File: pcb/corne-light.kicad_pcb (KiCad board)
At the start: 2 copper layers, 275.5 x 105.6 mm, 122 parts, among them J1 MJ-4PP-9, J2 OLED, J5 Breakaway_Tabs, J6 MJ-4PP-9, J7 OLED, SW1 SW_PUSH, SW10 SW_PUSH, SW11 SW_PUSH, SW12 SW_PUSH, SW13 SW_PUSH, SW14 SW_PUSH, SW15 SW_PUSH, SW16 SW_PUSH, SW17 SW_PUSH, SW18 SW_PUSH, SW19 Rotary_Encoder_Switch, SW2 SW_PUSH, SW20 SW_PUSH, SW21 SW_PUSH, SW22 SW_PUSH, SW23 SW_PUSH, SW24 SW_PUSH, SW25 SW_PUSH, SW26 SW_PUSH, SW27 SW_PUSH, SW28 SW_PUSH, SW29 SW_PUSH, SW3 SW_PUSH, SW30 SW_PUSH, SW31 SW_PUSH, SW32 SW_PUSH, SW33 SW_PUSH, SW34 SW_PUSH, SW35 SW_PUSH, SW36 SW_PUSH, SW37 SW_PUSH, SW38 SW_PUSH, SW39 SW_PUSH, SW4 SW_PUSH, SW40 Rotary_Encoder_Switch, SW41 SW_PUSH, SW42 SW_PUSH, SW5 SW_PUSH, SW6 SW_PUSH, SW7 SW_PUSH, SW8 SW_PUSH, SW9 SW_PUSH, U1 ProMicro, U2 ProMicro

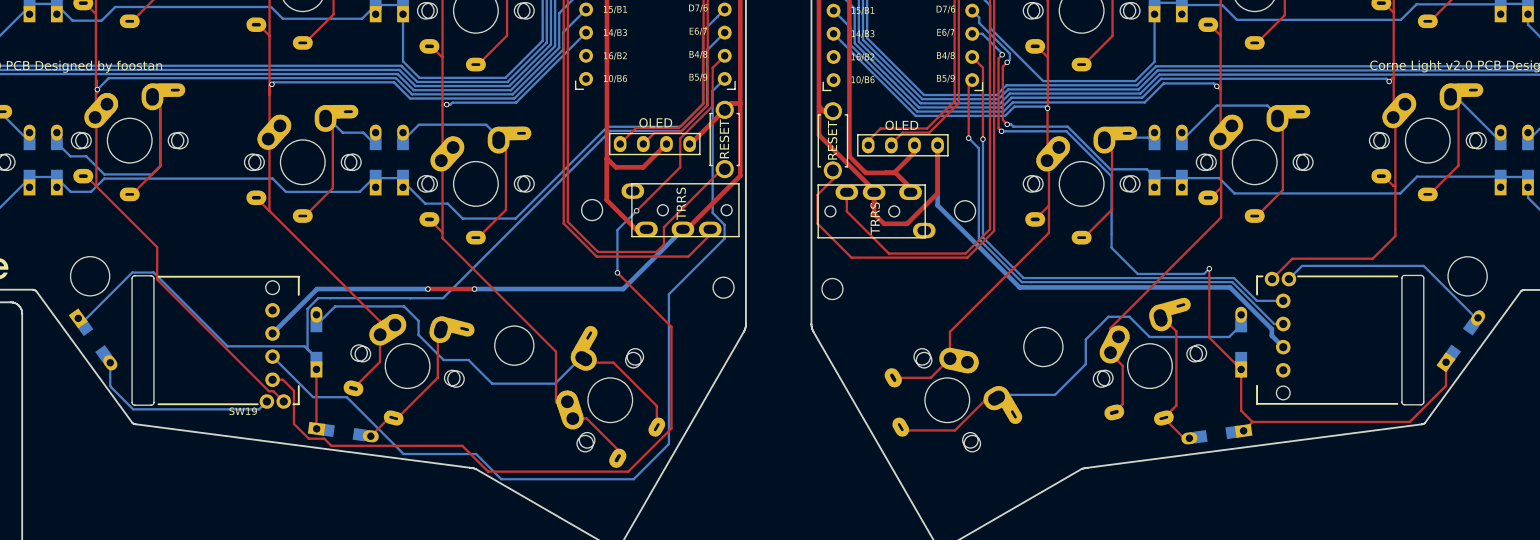
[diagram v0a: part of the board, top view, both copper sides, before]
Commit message: Update rotation and proper grounding
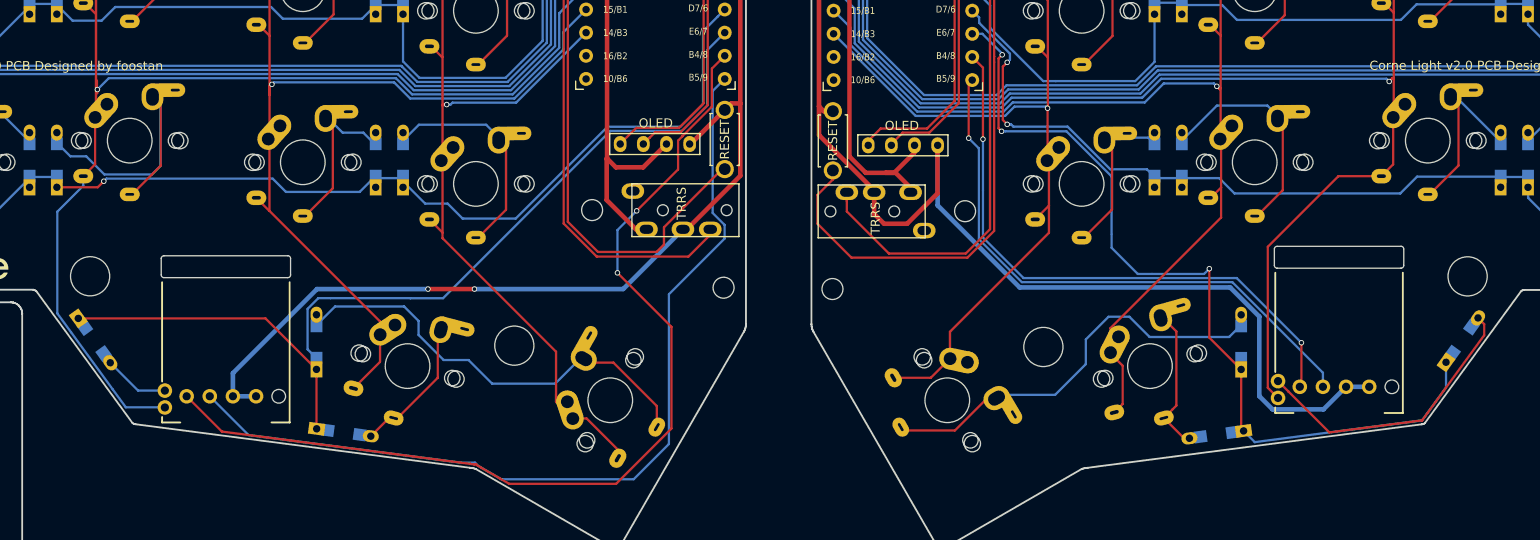
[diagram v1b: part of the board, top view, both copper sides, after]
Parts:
- turned SW19 to 90 degrees
- turned SW40 to 90 degrees
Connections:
- SW19 pad D: (no net) -> GND
- SW40 pad D: (no net) -> GNDA
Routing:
- net GNDA: track 129.5 -> 147.5 mm
- net Net-(D19-Pad2): track 21.2 -> 8.55 mm
- net GND: track 116.4 -> 127.6 mm
- net col3_r: track 143.4 -> 153.1 mm
- net ENCA_r: track 56.2 -> 65.0 mm, vias 1 -> 2
- net Net-(D40-Pad2): track 25.0 -> 33.8 mm
- net ENCB_r: track 55.4 -> 63.5 mm
- net ENCA: track 100.3 -> 106.4 mm
- net ENCB: track 94.4 -> 98.2 mm
- net row3: track 108.0 -> 106.3 mm
- net Net-(D20-Pad2): track 15.7 -> 17.0 mm
- net row3_r: track 96.6 -> 97.8 mm
- net col3: track 148.0 -> 146.9 mm
- net row2: track 153.9 -> 152.9 mm, vias 0 -> 1

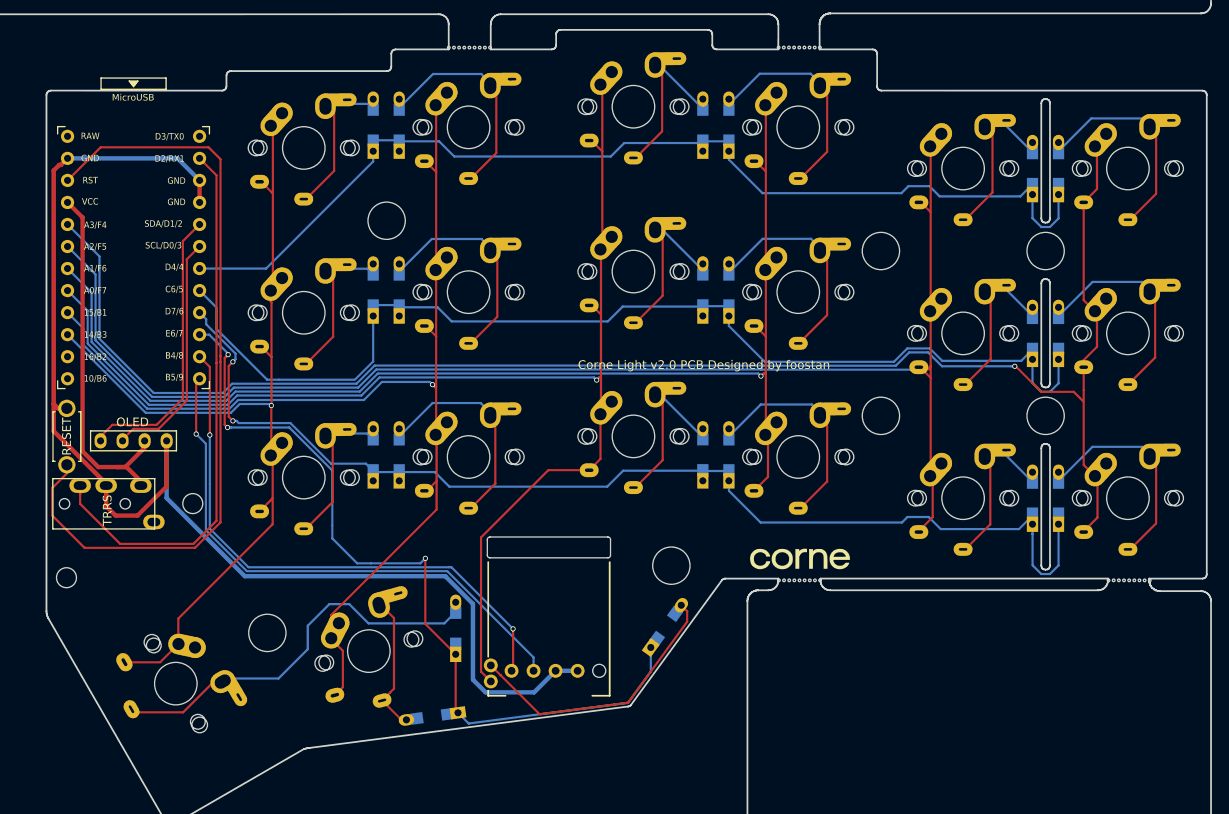
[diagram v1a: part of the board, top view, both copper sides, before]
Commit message: finish alps and leds on right half
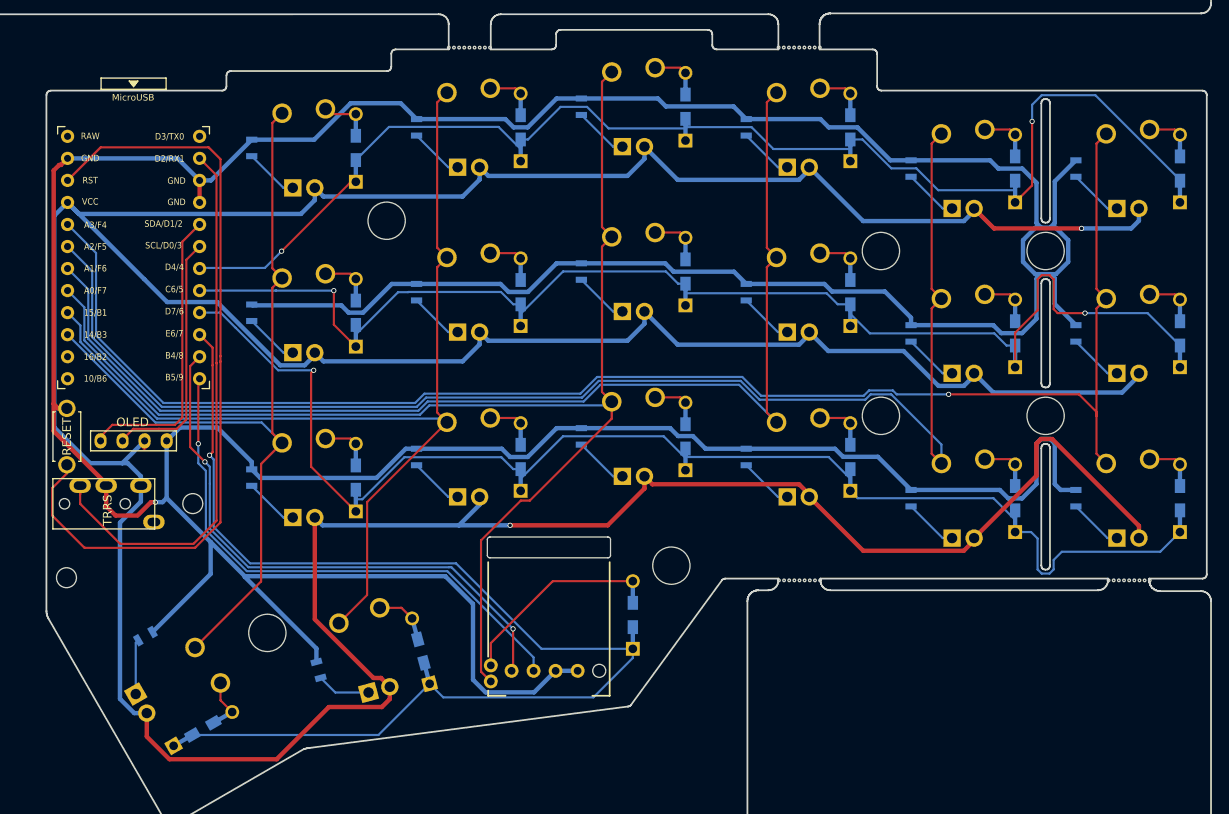
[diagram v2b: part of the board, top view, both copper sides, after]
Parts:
- removed D22, D23, D24, D25, D26, D27, D28, D29, D30, D31, D32, D33, D34, D35, D36, D37, D38, D39, D40, D41, D42: D, kbd:D3_TH_SMD_v2
- removed the G*** at (241.0, 91.0)
- removed the G*** at (240.8, 91.0)
- removed SW22, SW23, SW24, SW25, SW26, SW27, SW28, SW29, SW30, SW31, SW32, SW33, SW34, SW35, SW36, SW37, SW38, SW39, SW41: SW_PUSH, kbd:keyswitch_cherrymx_alps_choc12_1u
- removed SW42: SW_PUSH, kbd:keyswitch_cherrymx_alps_choc12_1.5u
- added D43: D_Small, Keebio-Parts:Diode-Hybrid-Back, F.Cu at (284.7, 45.9)
- added D44: D_Small, Keebio-Parts:Diode-Hybrid-Back, F.Cu at (284.7, 64.9)
- added D45: D_Small, Keebio-Parts:Diode-Hybrid-Back, F.Cu at (284.7, 83.9)
- added D46: D_Small, Keebio-Parts:Diode-Hybrid-Back, F.Cu at (265.7, 45.9)
- added D47: D_Small, Keebio-Parts:Diode-Hybrid-Back, F.Cu at (265.7, 64.9)
- added D48: D_Small, Keebio-Parts:Diode-Hybrid-Back, F.Cu at (265.7, 83.9)
- added D49: D_Small, Keebio-Parts:Diode-Hybrid-Back, F.Cu at (246.7, 41.2)
- added D50: D_Small, Keebio-Parts:Diode-Hybrid-Back, F.Cu at (246.7, 60.2)
- added D51: D_Small, Keebio-Parts:Diode-Hybrid-Back, F.Cu at (246.7, 79.2)
- added D52: D_Small, Keebio-Parts:Diode-Hybrid-Back, F.Cu at (227.7, 38.8)
- added D53: D_Small, Keebio-Parts:Diode-Hybrid-Back, F.Cu at (227.7, 57.8)
- added D54: D_Small, Keebio-Parts:Diode-Hybrid-Back, F.Cu at (227.7, 76.8)
- added D55: D_Small, Keebio-Parts:Diode-Hybrid-Back, F.Cu at (208.7, 41.2)
- added D56: D_Small, Keebio-Parts:Diode-Hybrid-Back, F.Cu at (208.7, 60.2)
- added D57: D_Small, Keebio-Parts:Diode-Hybrid-Back, F.Cu at (208.7, 79.2)
- added D58: D_Small, Keebio-Parts:Diode-Hybrid-Back, F.Cu at (189.7, 43.5)
- added D59: D_Small, Keebio-Parts:Diode-Hybrid-Back, F.Cu at (189.7, 62.5)
- added D60: D_Small, Keebio-Parts:Diode-Hybrid-Back, F.Cu at (189.7, 81.5)
- added D61: D_Small, Keebio-Parts:Diode-Hybrid-Back, F.Cu at (221.6, 97.4)
- added D62: D_Small, Keebio-Parts:Diode-Hybrid-Back, F.Cu at (197.2, 101.5)
- added D63: D_Small, Keebio-Parts:Diode-Hybrid-Back, F.Cu at (172.1, 110.5)
- added MX1: MX-LED, Alps_Only:ALPS-1U-LED, F.Cu at (278.7, 45.9)
- added MX10: MX-LED, Alps_Only:ALPS-1U-LED, F.Cu at (221.7, 38.8)
- added MX11: MX-LED, Alps_Only:ALPS-1U-LED, F.Cu at (221.7, 57.8)
- added MX12: MX-LED, Alps_Only:ALPS-1U-LED, F.Cu at (221.7, 76.8)
- added MX13: MX-LED, Alps_Only:ALPS-1U-LED, F.Cu at (202.7, 41.2)
- added MX14: MX-LED, Alps_Only:ALPS-1U-LED, F.Cu at (202.7, 60.2)
- added MX15: MX-LED, Alps_Only:ALPS-1U-LED, F.Cu at (202.7, 79.2)
- added MX16: MX-LED, Alps_Only:ALPS-1U-LED, F.Cu at (183.7, 43.5)
- added MX17: MX-LED, Alps_Only:ALPS-1U-LED, F.Cu at (183.7, 62.5)
- added MX18: MX-LED, Alps_Only:ALPS-1U-LED, F.Cu at (183.7, 81.5)
- added MX19: MX-LED, Alps_Only:ALPS-1U-LED, F.Cu at (191.2, 101.5)
- added MX2: MX-LED, Alps_Only:ALPS-1U-LED, F.Cu at (278.7, 64.9)
- added MX20: MX-LED, Alps_Only:ALPS-1.5U-LED, F.Cu at (168.9, 105.3)
- added MX3: MX-LED, Alps_Only:ALPS-1U-LED, F.Cu at (278.7, 83.9)
- added MX4: MX-LED, Alps_Only:ALPS-1U-LED, F.Cu at (259.7, 45.9)
- added MX5: MX-LED, Alps_Only:ALPS-1U-LED, F.Cu at (259.7, 64.9)
- added MX6: MX-LED, Alps_Only:ALPS-1U-LED, F.Cu at (259.7, 83.9)
- added MX7: MX-LED, Alps_Only:ALPS-1U-LED, F.Cu at (240.7, 41.2)
- added MX8: MX-LED, Alps_Only:ALPS-1U-LED, F.Cu at (240.7, 60.2)
- added MX9: MX-LED, Alps_Only:ALPS-1U-LED, F.Cu at (240.7, 79.2)
- added R1: 470, Keebio-Parts:R_0805, B.Cu at (272.7, 45.9)
- added R10: 470, Keebio-Parts:R_0805, B.Cu at (215.7, 38.8)
- added R11: 470, Keebio-Parts:R_0805, B.Cu at (215.7, 57.8)
- added R12: 470, Keebio-Parts:R_0805, B.Cu at (215.7, 76.8)
- added R13: 470, Keebio-Parts:R_0805, B.Cu at (196.7, 41.2)
- added R14: 470, Keebio-Parts:R_0805, B.Cu at (196.7, 60.2)
- added R15: 470, Keebio-Parts:R_0805, B.Cu at (196.7, 79.2)
- added R16: 470, Keebio-Parts:R_0805, B.Cu at (177.7, 43.5)
- added R17: 470, Keebio-Parts:R_0805, B.Cu at (177.7, 62.5)
- added R18: 470, Keebio-Parts:R_0805, B.Cu at (177.7, 81.5)
- added R19: 470, Keebio-Parts:R_0805, B.Cu at (185.4, 103.7)
- added R2: 470, Keebio-Parts:R_0805, B.Cu at (272.7, 64.9)
- added R20: 470, Keebio-Parts:R_0805, B.Cu at (165.4, 99.8)
- added R3: 470, Keebio-Parts:R_0805, B.Cu at (272.7, 83.9)
- added R4: 470, Keebio-Parts:R_0805, B.Cu at (253.7, 45.9)
- added R5: 470, Keebio-Parts:R_0805, B.Cu at (253.7, 64.9)
- added R6: 470, Keebio-Parts:R_0805, B.Cu at (253.7, 83.9)
- added R7: 470, Keebio-Parts:R_0805, B.Cu at (234.7, 41.2)
- added R8: 470, Keebio-Parts:R_0805, B.Cu at (234.7, 60.2)
- added R9: 470, Keebio-Parts:R_0805, B.Cu at (234.7, 79.2)
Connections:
- SW19 pad D: GND -> (no net)
- SW40 pad D: GNDA -> (no net)
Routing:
- net VDD: track 43.0 -> 539.2 mm, vias 0 -> 2
- net GNDA: track 147.5 -> 543.6 mm, vias 0 -> 1
- net Net-(D42-Pad2): track 47.8 -> 0.00 mm
- net row3_r: track 97.8 -> 134.1 mm, vias 3 -> 1
- net Net-(D24-Pad2): track 27.6 -> 0.00 mm
- net Net-(D32-Pad2): track 27.5 -> 0.00 mm
- net Net-(D26-Pad2): track 27.4 -> 0.00 mm
- net Net-(D38-Pad2): track 27.3 -> 0.00 mm
- net Net-(D36-Pad2): track 27.2 -> 0.00 mm
- net Net-(D34-Pad2): track 27.2 -> 0.00 mm
- net Net-(D30-Pad2): track 27.1 -> 0.00 mm
- net Net-(D22-Pad2): track 27.1 -> 0.00 mm
- net Net-(D28-Pad2): track 27.0 -> 0.00 mm
- net Net-(D31-Pad2): track 22.6 -> 0.00 mm
- net Net-(D25-Pad2): track 22.3 -> 0.00 mm
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
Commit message: add alps and leds to left half
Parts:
- removed G*** (x2): LOGO, kbd:corne-logo-horizontal
- removed SW10, SW11, SW12, SW13, SW14, SW15, SW16, SW17, SW18, SW2, SW20, SW3, SW4, SW5, SW6, SW7, SW8, SW9: SW_PUSH, kbd:keyswitch_cherrymx_alps_choc12_1u
- removed SW19: Rotary_Encoder_Switch, Encoder:RollerEncoder_Panasonic_EVQWGD001
- removed SW21: SW_PUSH, kbd:keyswitch_cherrymx_alps_choc12_1.5u
- added MX21: MX-LED, Alps_Only:ALPS-1U-LED, F.Cu at (22.2, 45.9)
- added MX22: MX-LED, Alps_Only:ALPS-1U-LED, F.Cu at (22.2, 64.9)
- added MX23: MX-LED, Alps_Only:ALPS-1U-LED, F.Cu at (22.2, 83.9)
- added MX24: MX-LED, Alps_Only:ALPS-1U-LED, F.Cu at (41.2, 45.9)
- added MX25: MX-LED, Alps_Only:ALPS-1U-LED, F.Cu at (41.2, 64.9)
- added MX26: MX-LED, Alps_Only:ALPS-1U-LED, F.Cu at (41.2, 83.9)
- added MX27: MX-LED, Alps_Only:ALPS-1U-LED, F.Cu at (60.2, 41.2)
- added MX28: MX-LED, Alps_Only:ALPS-1U-LED, F.Cu at (60.2, 60.2)
- added MX29: MX-LED, Alps_Only:ALPS-1U-LED, F.Cu at (60.2, 79.2)
- added MX30: MX-LED, Alps_Only:ALPS-1U-LED, F.Cu at (79.2, 38.8)
- added MX31: MX-LED, Alps_Only:ALPS-1U-LED, F.Cu at (79.2, 57.8)
- added MX32: MX-LED, Alps_Only:ALPS-1U-LED, F.Cu at (79.2, 76.8)
- added MX33: MX-LED, Alps_Only:ALPS-1U-LED, F.Cu at (98.2, 41.2)
- added MX34: MX-LED, Alps_Only:ALPS-1U-LED, F.Cu at (98.2, 60.2)
- added MX35: MX-LED, Alps_Only:ALPS-1U-LED, F.Cu at (98.2, 79.2)
- added MX36: MX-LED, Alps_Only:ALPS-1U-LED, F.Cu at (109.7, 101.5)
- added MX37: MX-LED, Alps_Only:ALPS-1U-LED, F.Cu at (117.2, 43.5)
- added MX38: MX-LED, Alps_Only:ALPS-1U-LED, F.Cu at (117.2, 62.5)
- added MX39: MX-LED, Alps_Only:ALPS-1U-LED, F.Cu at (117.2, 81.5)
- added MX40: MX-LED, Alps_Only:ALPS-1.5U-LED, F.Cu at (131.9, 105.3)
- added Q1: Q_NPN_BEC, Package_TO_SOT_SMD:SOT-23, B.Cu at (164.8, 43.4)
- added Q2: Q_NPN_BEC, Package_TO_SOT_SMD:SOT-23, B.Cu at (135.3, 42.0)
- added R21: 1k, Keebio-Parts:R_0805, B.Cu at (160.4, 44.3)
- added R22: 1k, Keebio-Parts:R_0805, B.Cu at (138.8, 42.0)
- added R23: 470, Keebio-Parts:R_0805, B.Cu at (16.2, 45.9)
- added R24: 470, Keebio-Parts:R_0805, B.Cu at (16.2, 64.9)
- added R25: 470, Keebio-Parts:R_0805, B.Cu at (16.2, 83.9)
- added R26: 470, Keebio-Parts:R_0805, B.Cu at (35.2, 45.9)
- added R27: 470, Keebio-Parts:R_0805, B.Cu at (35.2, 64.9)
- added R28: 470, Keebio-Parts:R_0805, B.Cu at (35.2, 83.9)
- added R29: 470, Keebio-Parts:R_0805, B.Cu at (54.2, 41.2)
- added R30: 470, Keebio-Parts:R_0805, B.Cu at (54.2, 60.2)
- added R31: 470, Keebio-Parts:R_0805, B.Cu at (54.2, 79.2)
- added R32: 470, Keebio-Parts:R_0805, B.Cu at (73.2, 38.8)
- added R33: 470, Keebio-Parts:R_0805, B.Cu at (73.2, 57.8)
- added R34: 470, Keebio-Parts:R_0805, B.Cu at (73.2, 76.8)
- added R35: 470, Keebio-Parts:R_0805, B.Cu at (92.2, 41.2)
- added R36: 470, Keebio-Parts:R_0805, B.Cu at (92.2, 60.2)
- added R37: 470, Keebio-Parts:R_0805, B.Cu at (92.2, 79.2)
- added R38: 470, Keebio-Parts:R_0805, B.Cu at (104.0, 100.4)
- added R39: 470, Keebio-Parts:R_0805, B.Cu at (111.2, 43.5)
- added R40: 470, Keebio-Parts:R_0805, B.Cu at (111.2, 62.5)
- added R41: 470, Keebio-Parts:R_0805, B.Cu at (111.2, 81.5)
- added R42: 470, Keebio-Parts:R_0805, B.Cu at (129.5, 110.6)
- D1, D10, D11, D12, D13, D14, D15, D16, D17, D18, D19, D2, D20, D21, D3, D4, D5, D6, D7, D8, D9: value D -> D_Small; footprint kbd:D3_TH_SMD_v2 -> Keebio-Parts:Diode-Hybrid-Back; moved to F.Cu
- SW1: value SW_PUSH -> Rotary_Encoder_Switch; footprint kbd:keyswitch_cherrymx_alps_choc12_1u -> Encoder:RollerEncoder_Panasonic_EVQWGD001
- moved SW1 85.7 mm to (89.3, 99.2), turned to 90 degrees
- moved D14 82.9 mm to (104.2, 41.2), turned to 270 degrees
- moved D6 75.5 mm to (47.2, 83.9), turned to 270 degrees
- moved D5 63.7 mm to (47.2, 64.9), turned to 270 degrees
- moved D19 60.0 mm to (123.2, 62.5), turned to 270 degrees
- moved D3 58.7 mm to (28.2, 83.9), turned to 270 degrees
- moved D13 51.8 mm to (80.2, 97.6)
- moved D7 43.1 mm to (66.2, 41.2), turned to 270 degrees
- moved D15 40.6 mm to (104.2, 60.2), turned to 270 degrees
- moved D18 38.0 mm to (123.2, 43.5), turned to 270 degrees
- moved D21 35.3 mm to (135.0, 100.2), turned to 330 degrees
- moved D20 34.1 mm to (123.2, 81.5), turned to 270 degrees
- moved D8 33.3 mm to (66.2, 60.2), turned to 270 degrees
- moved D16 33.0 mm to (104.2, 79.2), turned to 270 degrees
- moved D12 29.3 mm to (85.2, 76.8), turned to 270 degrees
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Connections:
- D10 pad 1: row1 -> row0
- D12 pad 1: row1 -> row2
- D13 pad 1: row2 -> row3
- D14 pad 1: row2 -> row0
- D15 pad 1: row2 -> row1
- D17 pad 1: row2 -> row3
- D18 pad 1: row2 -> row0
- D19 pad 1: row3 -> row1
- D2 pad 1: row0 -> row1
- D20 pad 1: row3 -> row2
- D3 pad 1: row0 -> row2
- D5 pad 1: row0 -> row1
- D6 pad 1: row0 -> row2
- D7 pad 1: row1 -> row0
- D9 pad 1: row1 -> row2
- R1 pad 2: GNDA -> PWM_r
- R10 pad 2: GNDA -> PWM_r
- R11 pad 2: GNDA -> PWM_r
- R12 pad 2: GNDA -> PWM_r
- R13 pad 2: GNDA -> PWM_r
- R14 pad 2: GNDA -> PWM_r
- R15 pad 2: GNDA -> PWM_r
- R16 pad 2: GNDA -> PWM_r
- R17 pad 2: GNDA -> PWM_r
- R18 pad 2: GNDA -> PWM_r
- R19 pad 2: GNDA -> PWM_r
- R2 pad 2: GNDA -> PWM_r
- R20 pad 2: GNDA -> PWM_r
- R3 pad 2: GNDA -> PWM_r
- R4 pad 2: GNDA -> PWM_r
- R5 pad 2: GNDA -> PWM_r
- R6 pad 2: GNDA -> PWM_r
- R7 pad 2: GNDA -> PWM_r
- R8 pad 2: GNDA -> PWM_r
- R9 pad 2: GNDA -> PWM_r
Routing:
- net PWM: track 0.00 -> 446.6 mm, vias 0 -> 6
- net VCC: track 48.3 -> 490.5 mm, vias 0 -> 2
- net PWM_r: track 0.00 -> 429.0 mm, vias 0 -> 3
- net GNDA: track 543.6 -> 146.0 mm, vias 1 -> 0
- net Net-(D21-Pad2): track 49.4 -> 4.48 mm
- net Net-(R22-Pad2): track 0.00 -> 35.2 mm, vias 0 -> 2
- net data: track 78.9 -> 44.5 mm
- net Net-(D16-Pad2): track 35.7 -> 5.28 mm
- net Net-(R21-Pad2): track 0.00 -> 27.1 mm, vias 0 -> 1
- net col0: track 182.3 -> 155.4 mm, vias 1 -> 0
- net row1: track 164.0 -> 137.8 mm, vias 0 -> 1
- net Net-(D4-Pad2): track 29.0 -> 5.30 mm
- net Net-(D10-Pad2): track 27.9 -> 5.24 mm
- net Net-(D14-Pad2): track 27.9 -> 5.28 mm
- net Net-(D2-Pad2): track 27.4 -> 5.26 mm
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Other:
- board text removed: "Corne Light v2.0 PCB Designed by foostan"

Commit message: Finish RGB
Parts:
- added LED1: YS-SK6812MINI-E, Keebio-Parts:SK6812-MINI-E, F.Cu at (163.8, 63.1)
- added LED10: YS-SK6812MINI-E, Keebio-Parts:SK6812-MINI-E, F.Cu at (86.6, 46.7)
- added LED2: YS-SK6812MINI-E, Keebio-Parts:SK6812-MINI-E, F.Cu at (167.5, 93.1)
- added LED3: YS-SK6812MINI-E, Keebio-Parts:SK6812-MINI-E, F.Cu at (233.7, 87.8)
- added LED4: YS-SK6812MINI-E, Keebio-Parts:SK6812-MINI-E, F.Cu at (241.6, 51.7)
- added LED5: YS-SK6812MINI-E, Keebio-Parts:SK6812-MINI-E, F.Cu at (204.5, 52.0)
- added LED6: YS-SK6812MINI-E, Keebio-Parts:SK6812-MINI-E, F.Cu at (136.4, 54.8)
- added LED7: YS-SK6812MINI-E, Keebio-Parts:SK6812-MINI-E, F.Cu at (121.7, 93.4)
- added LED8: YS-SK6812MINI-E, Keebio-Parts:SK6812-MINI-E, F.Cu at (66.3, 88.8)
- added LED9: YS-SK6812MINI-E, Keebio-Parts:SK6812-MINI-E, F.Cu at (64.7, 69.8)
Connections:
- U1 pad 1: Net-(U1-Pad1) -> DIN
- U2 pad 1: Net-(U2-Pad1) -> DIN_r
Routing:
- net GND: track 128.5 -> 251.5 mm, vias 1 -> 6
- net GNDA: track 146.0 -> 267.4 mm, vias 0 -> 7
- net Net-(LED2-Pad2): track 0.00 -> 72.1 mm, vias 0 -> 2
- net Net-(LED6-Pad2): track 0.00 -> 67.4 mm, vias 0 -> 2
- net Net-(LED7-Pad2): track 0.00 -> 67.2 mm, vias 0 -> 2
- net reset_r: track 90.3 -> 34.4 mm
- net Net-(LED4-Pad2): track 0.00 -> 51.2 mm, vias 0 -> 2
- net Net-(LED3-Pad2): track 0.00 -> 48.7 mm
- net Net-(LED1-Pad2): track 0.00 -> 40.3 mm, vias 0 -> 2
- net Net-(LED8-Pad2): track 0.00 -> 38.5 mm, vias 0 -> 2
- net VCC: track 490.5 -> 528.7 mm, vias 2 -> 4
- net Net-(LED10-Pad4): track 0.00 -> 38.0 mm, vias 0 -> 2
- net VDD: track 538.5 -> 569.0 mm, vias 2 -> 4
- net DIN_r: track 0.00 -> 23.8 mm
- net DIN: track 0.00 -> 15.7 mm
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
